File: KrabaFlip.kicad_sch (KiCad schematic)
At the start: 4 parts, among them J2 USB4105GFA120, U3 CM5108032

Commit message: Add DSI, JST-PH connectors
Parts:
- added J1: 522711369, 522711369:CON_522711369_MOL, symbol 2025-11-29_14-12-47:522711369
- added J3: S2B-PH-K-SLFSN, S2B-PH-K-S-LF-SN:CONN_S2B-PH-K-S_JST, symbol 2025-11-29_14-43-49:S2B-PH-K-SLFSN
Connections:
- net +3V3: now also J1.P1, J1.P2
- net GND: now also J1.1, J1.10, J1.13, J1.4, J1.7
- net SCL0: now reaches U3.80 (SCL0)
- net SCL0: now also J1.11
- net SDA0: now reaches U3.82 (SDA0)
- net SDA0: now also J1.12
- net DSI1_DP0: now reaches U3.175 (MIPI1_D0_N)
- net DSI1_DP0: now also J1.9
- net DSI1_DN0: now reaches U3.177 (MIPI1_D0_P)
- net DSI1_DN0: now also J1.8
- net DSI1_DN1: now reaches U3.181 (MIPI1_D1_N)
- net DSI1_DN1: now also J1.2
- net DSI1_DP1: now reaches U3.183 (MIPI1_D1_P)
- net DSI1_DP1: now also J1.3
- net DSI1_CN: now reaches U3.187 (MIPI1_C_N)
- net DSI1_CN: now also J1.5
- net DSI1_CP: now reaches U3.189 (MIPI1_C_P)
- net DSI1_CP: now also J1.6
- no-connect marks 17 -> 15

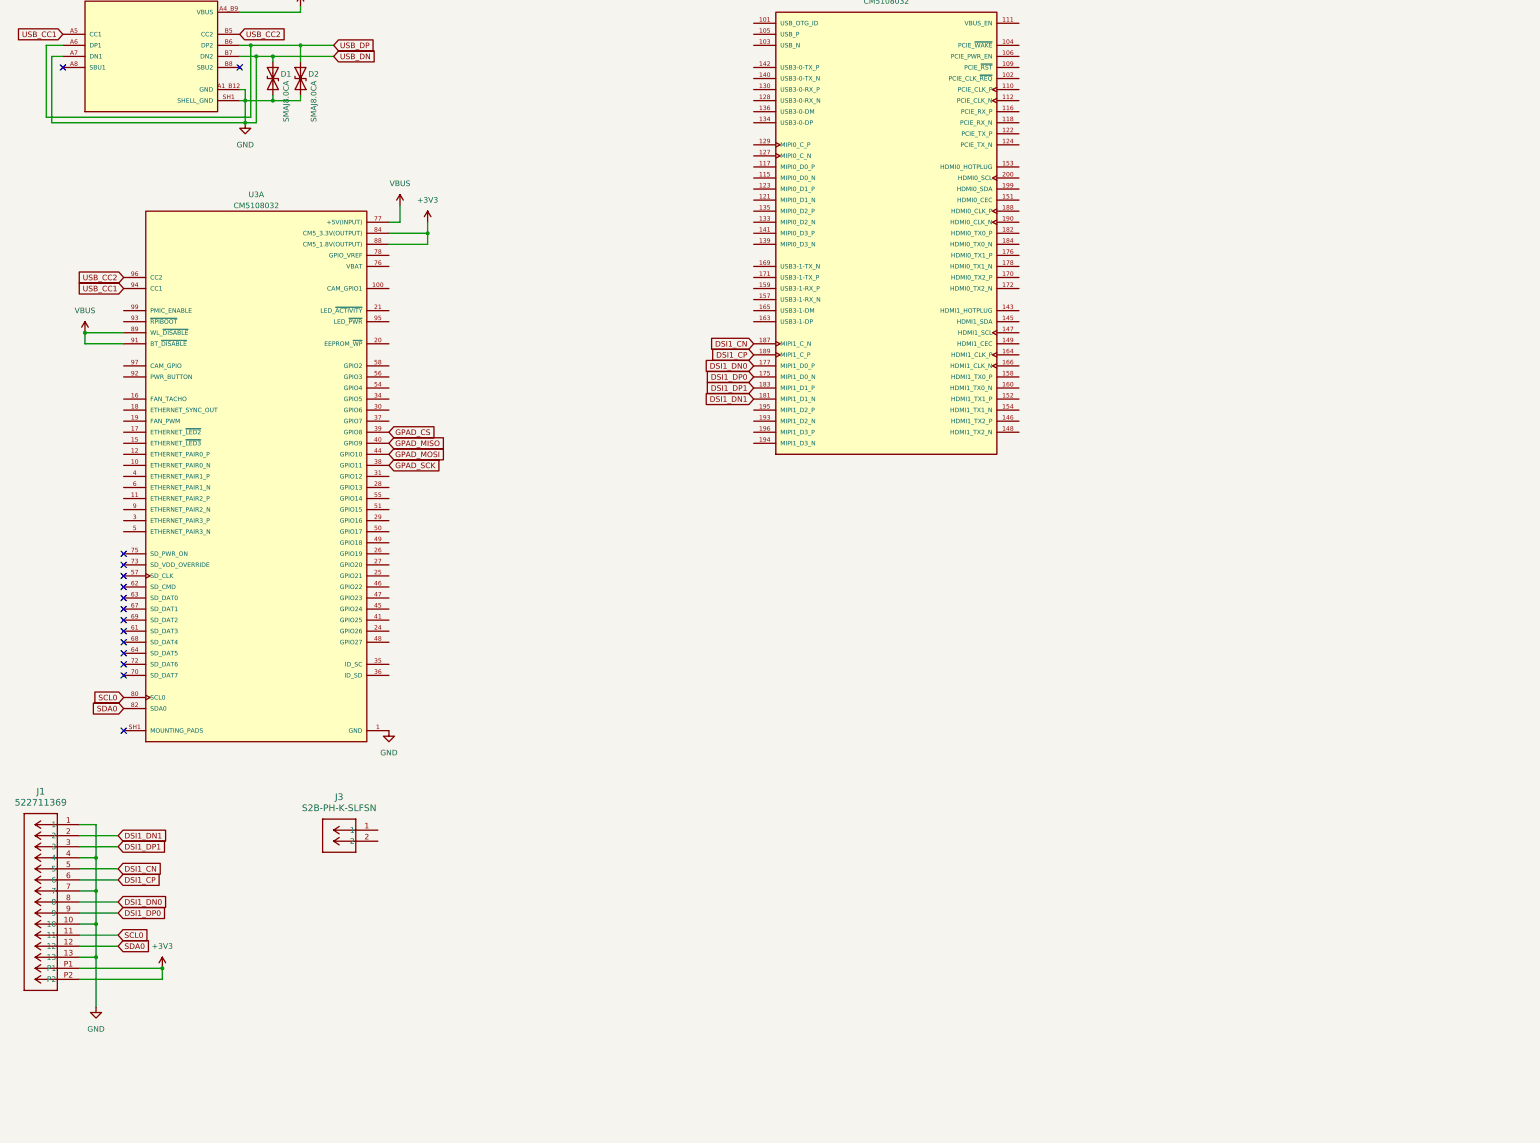
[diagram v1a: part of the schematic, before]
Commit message: Add joystick connectors
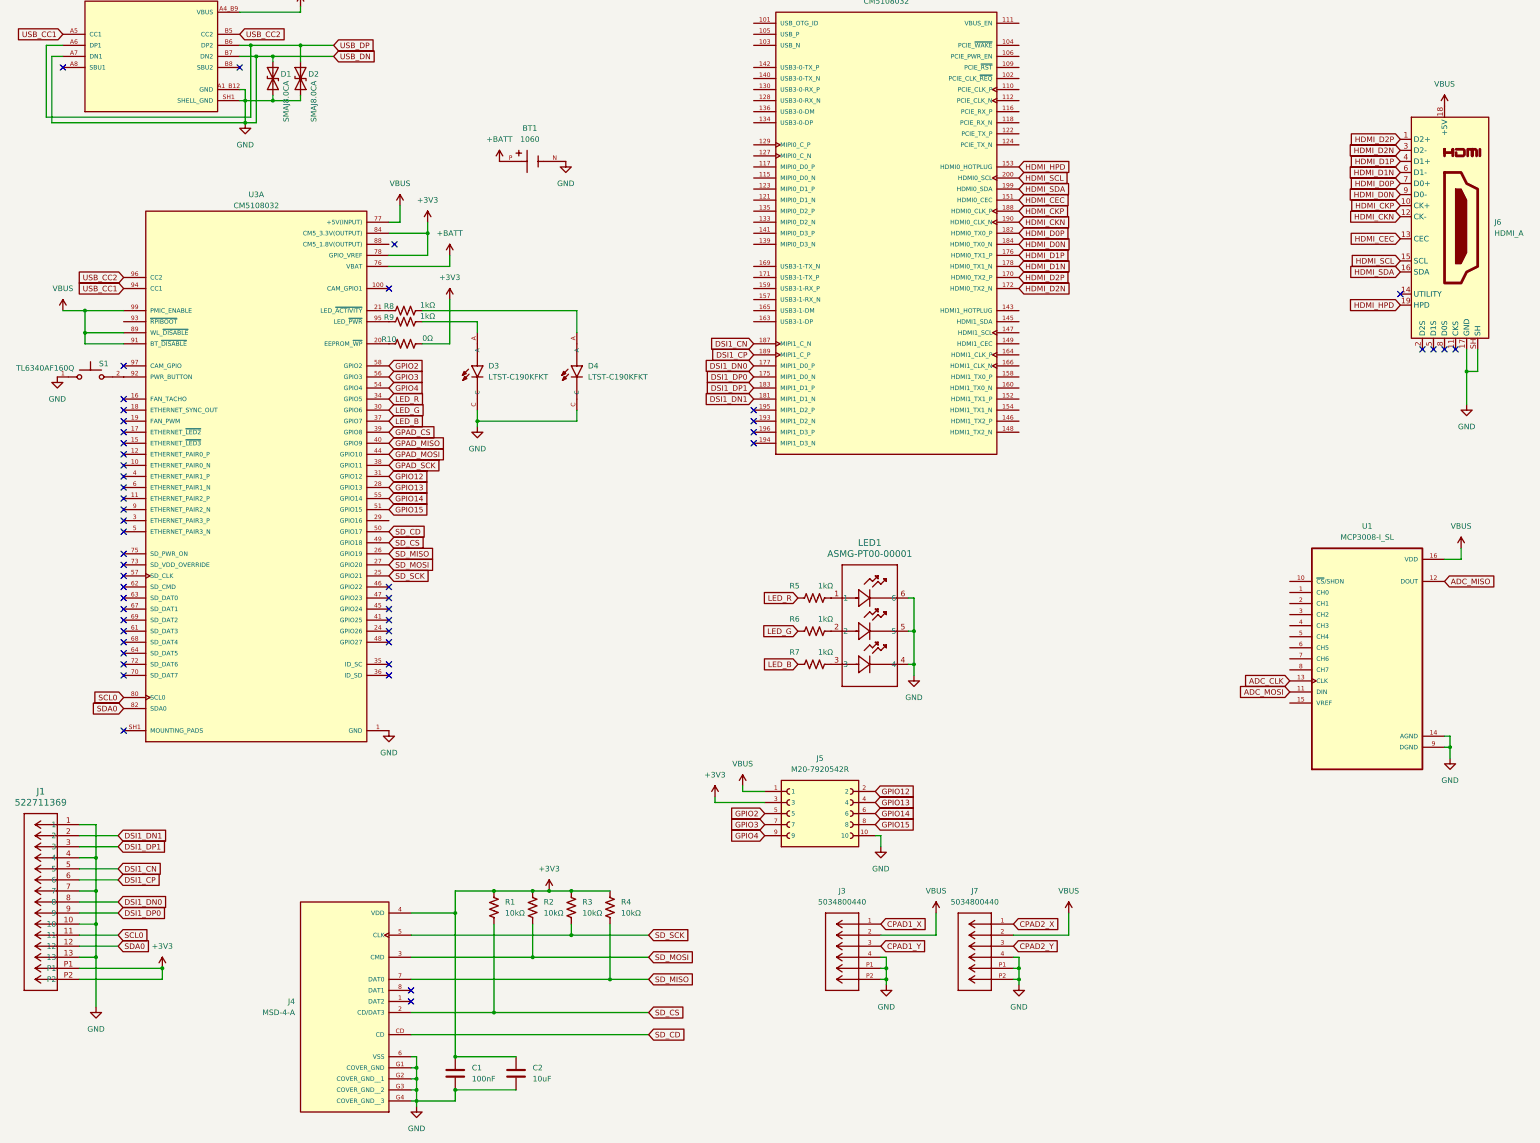
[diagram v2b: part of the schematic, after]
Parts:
- removed J3: S2B-PH-K-SLFSN, S2B-PH-K-S-LF-SN:CONN_S2B-PH-K-S_JST, symbol 2025-11-29_14-43-49:S2B-PH-K-SLFSN
- added BT1: 1060, 1060:BAT_1060, symbol 1060:1060
- added C1: 100nF, Capacitor_SMD:C_0402_1005Metric, symbol Device:C
- added C2: 10uF, Capacitor_SMD:C_0402_1005Metric, symbol Device:C
- added D3, D4: LTST-C190KFKT, LTST-C190KFKT:LEDM1608X80, symbol LTST-C190KFKT:LTST-C190KFKT
- added J3, J7: 5034800440, 5034800440:CON_5034800440_MOL, symbol 5034800440:5034800440
- added J4: MSD-4-A, MSD_4_A:CUI_MSD-4-A, symbol MSD-4-A:MSD-4-A
- added J5: M20-7920542R, M20-7920542R:HARWIN_M20-7920542R, symbol M20-7920542R:M20-7920542R
- added J6: HDMI_A, Connector_Video:HDMI_A_Amphenol_10029449-x01xLF_Horizontal, symbol Connector:HDMI_A
- added LED1: ASMG-PT00-00001, ASMG-PT00-00001:ASMG-PT00_BRA, symbol 2025-11-30_06-53-48:ASMG-PT00-00001
- added R1, R2, R3, R4: 10kΩ, Resistor_SMD:R_0402_1005Metric, symbol Device:R_US
- added R10: 0Ω, Resistor_SMD:R_0402_1005Metric, symbol Device:R_US
- added R5, R6, R7, R8, R9: 1kΩ, Resistor_SMD:R_0402_1005Metric, symbol Device:R_US
- added S1: TL6340AF160Q, TL6340AF160Q:SW_TL6340AF160Q, symbol TL6340AF160Q:TL6340AF160Q
- added U1: MCP3008-I_SL, MCP3008-I_SL:SOIC127P600X175-16N, symbol MCP3008-I_SL:MCP3008-I_SL
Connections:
- net +3V3: now also U3.78 (GPIO_VREF), C1.1, C2.1, J4.4 (VDD), J5.3, R1.1, R10.2, R2.1, R3.1, R4.1; no longer U3.88 (CM5_1.8V(OUTPUT)), U3.90 (CM5_1.8V(OUTPUT))
- net +5V(INPUT): now also U3.99 (PMIC_ENABLE), J3.2, J5.1, J6.18 (+5V), J7.2, U1.16 (VDD)
- net GND: now also BT1.N, C1.2, C2.2, D3.C, D4.C, J3.4, J3.P1, J3.P2, J4.6 (VSS), J4.G1 (COVER_GND), J4.G2 (COVER_GND__1), J4.G3 (COVER_GND__2), J4.G4 (COVER_GND__3), J5.10, J6.17 (GND), J6.SH, J7.4, J7.P1, J7.P2, LED1.4, LED1.5, LED1.6, S1.1, U1.14 (AGND), U1.9 (DGND)
- net at U3.20 (EEPROM_~{WP}): now also R10.1
- net at U3.21 (LED_~{ACTIVITY}): now also R8.1
- net SD_SCK: now reaches U3.25 (GPIO21)
- net SD_SCK: now also J4.5 (CLK), R3.2
- net SD_MISO: now reaches U3.26 (GPIO19)
- net SD_MISO: now also J4.7 (DAT0), R4.2
- net SD_MOSI: now reaches U3.27 (GPIO20)
- net SD_MOSI: now also J4.3 (CMD), R2.2
- net GPIO13: now reaches U3.28 (GPIO13)
- net GPIO13: now also J5.4
- net LED_G: now reaches U3.30 (GPIO6)
- net LED_G: now also R6.1
- net GPIO12: now reaches U3.31 (GPIO12)
- net GPIO12: now also J5.2
- net LED_R: now reaches U3.34 (GPIO5)
- net LED_R: now also R5.1
- net LED_B: now reaches U3.37 (GPIO7)
- net LED_B: now also R7.1
- net SD_CS: now reaches U3.49 (GPIO18)
- net SD_CS: now also J4.2 (CD/DAT3), R1.2
- net SD_CD: now reaches U3.50 (GPIO17)
- net SD_CD: now also J4.CD
- net GPIO15: now reaches U3.51 (GPIO15)
- net GPIO15: now also J5.8
- net GPIO4: now reaches U3.54 (GPIO4)
- net GPIO4: now also J5.9
- net GPIO14: now reaches U3.55 (GPIO14)
- net GPIO14: now also J5.6
- net GPIO3: now reaches U3.56 (GPIO3)
- net GPIO3: now also J5.7
- net GPIO2: now reaches U3.58 (GPIO2)
- net GPIO2: now also J5.5
- net +BATT: now reaches U3.76 (VBAT)
- net +BATT: now also BT1.P
- net at U3.92 (PWR_BUTTON): now also S1.2
- net at U3.95 (LED_~{PWR}): now also R9.1
- net HDMI_CEC: now reaches U3.151 (HDMI0_CEC)
- net HDMI_CEC: now also J6.13 (CEC)
- net HDMI_HPD: now reaches U3.153 (HDMI0_HOTPLUG)
- net HDMI_HPD: now also J6.19 (HPD)
- net HDMI_D2P: now reaches U3.170 (HDMI0_TX2_P)
- net HDMI_D2P: now also J6.1 (D2+)
- net HDMI_D2N: now reaches U3.172 (HDMI0_TX2_N)
- net HDMI_D2N: now also J6.3 (D2-)
- net HDMI_D1P: now reaches U3.176 (HDMI0_TX1_P)
- net HDMI_D1P: now also J6.4 (D1+)
- net HDMI_D1N: now reaches U3.178 (HDMI0_TX1_N)
- net HDMI_D1N: now also J6.6 (D1-)
- net HDMI_D0P: now reaches U3.182 (HDMI0_TX0_P)
- net HDMI_D0P: now also J6.7 (D0+)
- net HDMI_D0N: now reaches U3.184 (HDMI0_TX0_N)
- net HDMI_D0N: now also J6.9 (D0-)
- net HDMI_CKP: now reaches U3.188 (HDMI0_CLK_P)
- net HDMI_CKP: now also J6.10 (CK+)
- net HDMI_CKN: now reaches U3.190 (HDMI0_CLK_N)
- net HDMI_CKN: now also J6.12 (CK-)
- net HDMI_SDA: now reaches U3.199 (HDMI0_SDA)
- net HDMI_SDA: now also J6.16 (SDA)
- net HDMI_SCL: now reaches U3.200 (HDMI0_SCL)
- net HDMI_SCL: now also J6.15 (SCL)
- new net: LED1.1, R5.2
- new net: LED1.2, R6.2
- new net: LED1.3, R7.2
- new net: D4.A, R8.2
- new net: D3.A, R9.2
- new net ADC_CLK: U1.13 (CLK)
- new net ADC_MISO: U1.12 (DOUT)
- new net ADC_MOSI: U1.11 (DIN)
- new net CM5_1.8V(OUTPUT): U3.88 (CM5_1.8V(OUTPUT)), U3.90 (CM5_1.8V(OUTPUT))
- new net CPAD1_X: J3.1
- new net CPAD1_Y: J3.3
- new net CPAD2_X: J7.1
- new net CPAD2_Y: J7.3
- no-connect marks 15 -> 50

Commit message: Add KrabaFlip.kicad_pcb
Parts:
- removed J5: M20-7920542R, M20-7920542R:HARWIN_M20-7920542R, symbol M20-7920542R:M20-7920542R
- added R11, R12, R13, R14, R15, R16, R17, R18: 10kΩ, Resistor_SMD:R_0402_1005Metric, symbol Device:R_US
- added S2, S3, S4, S5, S6, S7, S8, S9: B3F-4050, B3F_4050:SW_B3F-4050, symbol B3F-4050:B3F-4050
- added U2: TXS0108ERGYR, TXS0108ERGYR:IC_TXS0108ERGYR, symbol TXS0108ERGYR:TXS0108ERGYR
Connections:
- net +3V3: now also U3.111 (VBUS_EN), U3.89 (WL_~{DISABLE}), U3.91 (BT_~{DISABLE}), U3.99 (PMIC_ENABLE), R11.2, R12.2, R13.2, R14.2, R15.2, R16.2, R17.2, R18.2, U2.10 (OE), U2.2 (VCCA)
- net +5V(INPUT): now also U1.15 (VREF), U2.19 (VCCB); no longer U3.89 (WL_~{DISABLE}), U3.91 (BT_~{DISABLE}), U3.99 (PMIC_ENABLE)
- net ADC_CLK: now also U2.20 (B1)
- net ADC_MISO: now also U2.17 (B3)
- net ADC_MOSI: now also U2.18 (B2)
- net CPAD1_X: now also U1.1 (CH0)
- net CPAD1_Y: now also U1.2 (CH1)
- net CPAD2_X: now also U1.3 (CH2)
- net CPAD2_Y: now also U1.4 (CH3)
- net GND: now also S2.3, S2.4, S3.3, S3.4, S4.3, S4.4, S5.3, S5.4, S6.3, S6.4, S7.3, S7.4, S8.3, S8.4, S9.3, S9.4, U2.11 (GND), U2.21 (EXP); no longer D1.2 (A2), J2.A7 (DN1), J2.B7 (DN2)
- net ADC_CS: now reaches U1.10 (~{CS}/SHDN)
- net BUTTON_X: now reaches U3.24 (GPIO26)
- net BUTTON_X: now also R12.1, S2.1, S2.2
- net BUTTON_A: now reaches U3.29 (GPIO16)
- net BUTTON_A: now also R13.1, S3.1, S3.2
- net BUTTON_B: now reaches U3.41 (GPIO25)
- net BUTTON_B: now also R14.1, S5.1, S5.2
- net ADC_3V3_MISO: now reaches U3.45 (GPIO24)
- net ADC_3V3_MISO: now also U2.4 (A3)
- net ADC_3V3_CLK: now reaches U3.46 (GPIO22)
- net ADC_3V3_CLK: now also U2.1 (A1)
- net ADC_3V3_MOSI: now reaches U3.47 (GPIO23)
- net ADC_3V3_MOSI: now also U2.3 (A2)
- net BUTTON_Y: now reaches U3.48 (GPIO27)
- net BUTTON_Y: now also R11.1, S4.1, S4.2
- net GPIO12 renamed BUTTON_UP
- net BUTTON_UP: now also R15.1, S6.1, S6.2
- net GPIO13 renamed BUTTON_DWN
- net BUTTON_DWN: now also R16.1, S7.1, S7.2
- net GPIO14 renamed BUTTON_LFT
- net BUTTON_LFT: now also R17.1, S8.1, S8.2
- net GPIO15 renamed BUTTON_RGT
- net BUTTON_RGT: now also R18.1, S9.1, S9.2
- net GPIO2: no longer names the net of U3.58 (GPIO2)
- net GPIO3: no longer names the net of U3.56 (GPIO3)
- net GPIO4: no longer names the net of U3.54 (GPIO4)
- new net USB_DN: D1.2 (A2), J2.A7 (DN1), J2.B7 (DN2)
- no-connect marks 50 -> 108
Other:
- moved on the sheet: J6, U1
